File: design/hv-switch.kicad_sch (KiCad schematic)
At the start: 28 parts, among them Q3 GAN080-650EBE, U6 MAX22701DASA+, U7 MAX22702EASA+

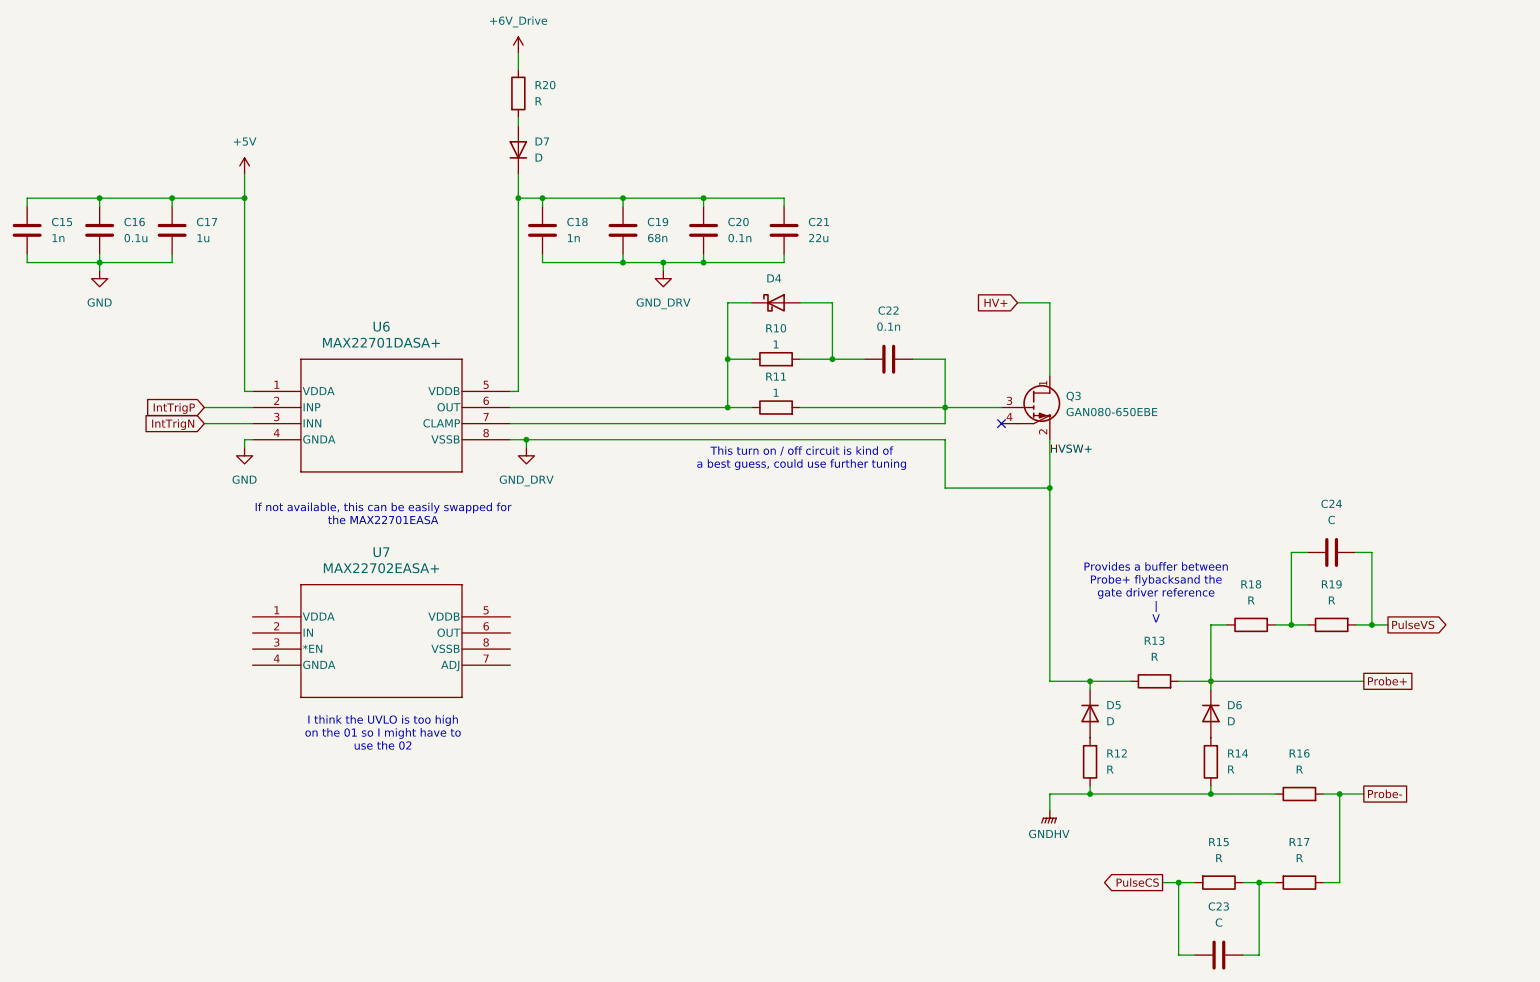
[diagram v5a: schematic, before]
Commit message: Fixed gate drive UVLO
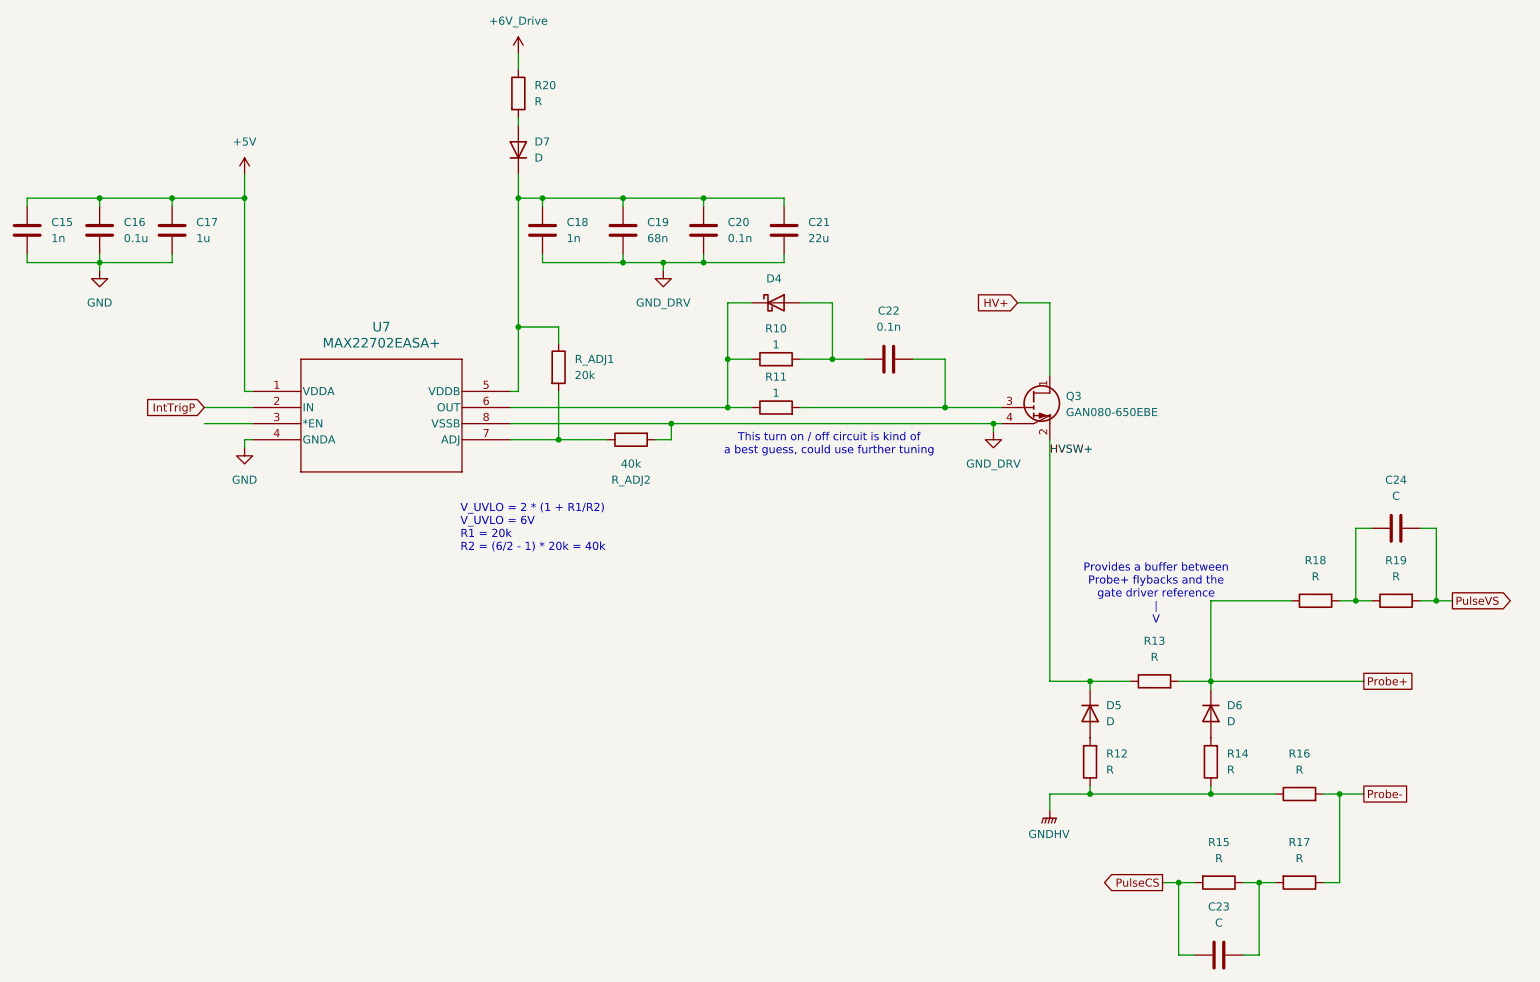
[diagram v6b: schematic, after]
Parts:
- removed U6: MAX22701DASA+, project-footprints:21-0041-A_8L, symbol project_symbols:MAX22701DASA+
- added R_ADJ1: 20k, symbol Device:R
- added R_ADJ2: 40k, symbol Device:R
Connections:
- net +5V: now also U7.1 (VDDA)
- net GND: now also U7.4 (GNDA)
- net GND_DRV: now also Q3.4 (SS), U7.8 (VSSB), R_ADJ2.2; no longer D5.1 (K), Q3.2 (S), R13.1
- net IntTrigP: now also U7.2 (IN)
- net at C18.1, C19.1, C20.1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: now also U7.5 (VDDB), R_ADJ1.1
- net at D4.1 (K), R10.1, R11.1: now also U7.6 (OUT)
- net at U7.7 (ADJ): now also R_ADJ1.2, R_ADJ2.1
- new net HVSW+: D5.1 (K), Q3.2 (S), R13.1
- no-connect marks 1 -> 0
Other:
- note added: "Provides a buffer between Probe+ flybacks and the gate driver reference | V"
- note added: "V_UVLO = 2 * (1 + R1/R2) V_UVLO = 6V R1 = 20k R2 = (6/2 - 1) * 20k = 40k"
- note removed: "I think the UVLO is too high on the 01 so I might have to use the 02"
- note removed: "If not available, this can be easily swapped for the MAX22701EASA"
- note removed: "Provides a buffer between Probe+ flybacksand the gate driver reference | V"
- moved on the sheet: C24, R18, R19, U7

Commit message: _
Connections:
- net PulseEN: now reaches U7.3 (*EN)
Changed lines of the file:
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@@
+		)
+	)
+	(global_label "PulseEN"
+		(shape input)
+		(at 62.23 78.74 180)
+		(fields_autoplaced yes)
+		(effects
+			(font
+				(size 1.27 1.27)
+			)
+			(justify right)
+		)
+		(property "Intersheetrefs" "${INTERSHEET_REFS}"
+			(at 51.5644 78.74 0)
+			(effects
+				(font
+					(size 1.27 1.27)
+				)
+				(justify right)
+				(hide yes)
+			)
 		)
 	)

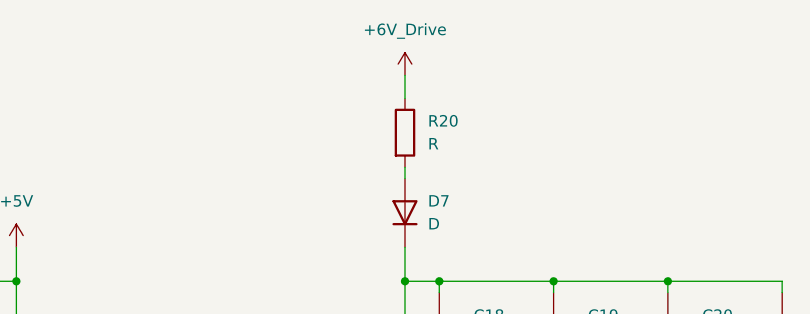
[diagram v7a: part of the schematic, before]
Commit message: Almost finished primary power regulation
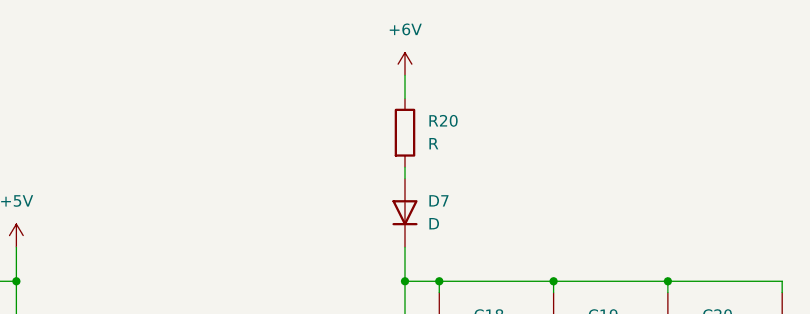
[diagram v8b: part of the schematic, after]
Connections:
- net +6V_Drive renamed +6V
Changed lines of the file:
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@@
 			)
 		)
-		(property "Value" "+6V_Drive"
+		(property "Value" "+6V"
 			(at 111.76 15.24 0)
 			(effects
